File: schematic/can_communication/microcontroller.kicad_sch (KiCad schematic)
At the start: 1 part, among them U1 STM32H723ZGTx

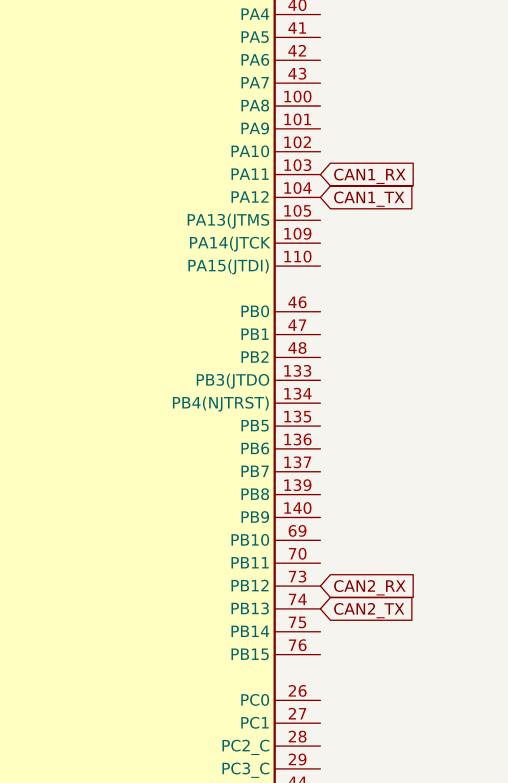
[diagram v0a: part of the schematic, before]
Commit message: added usb connectors
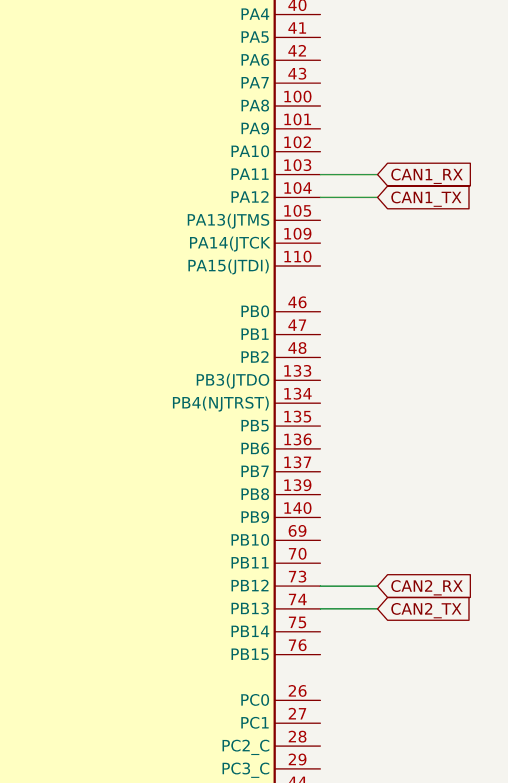
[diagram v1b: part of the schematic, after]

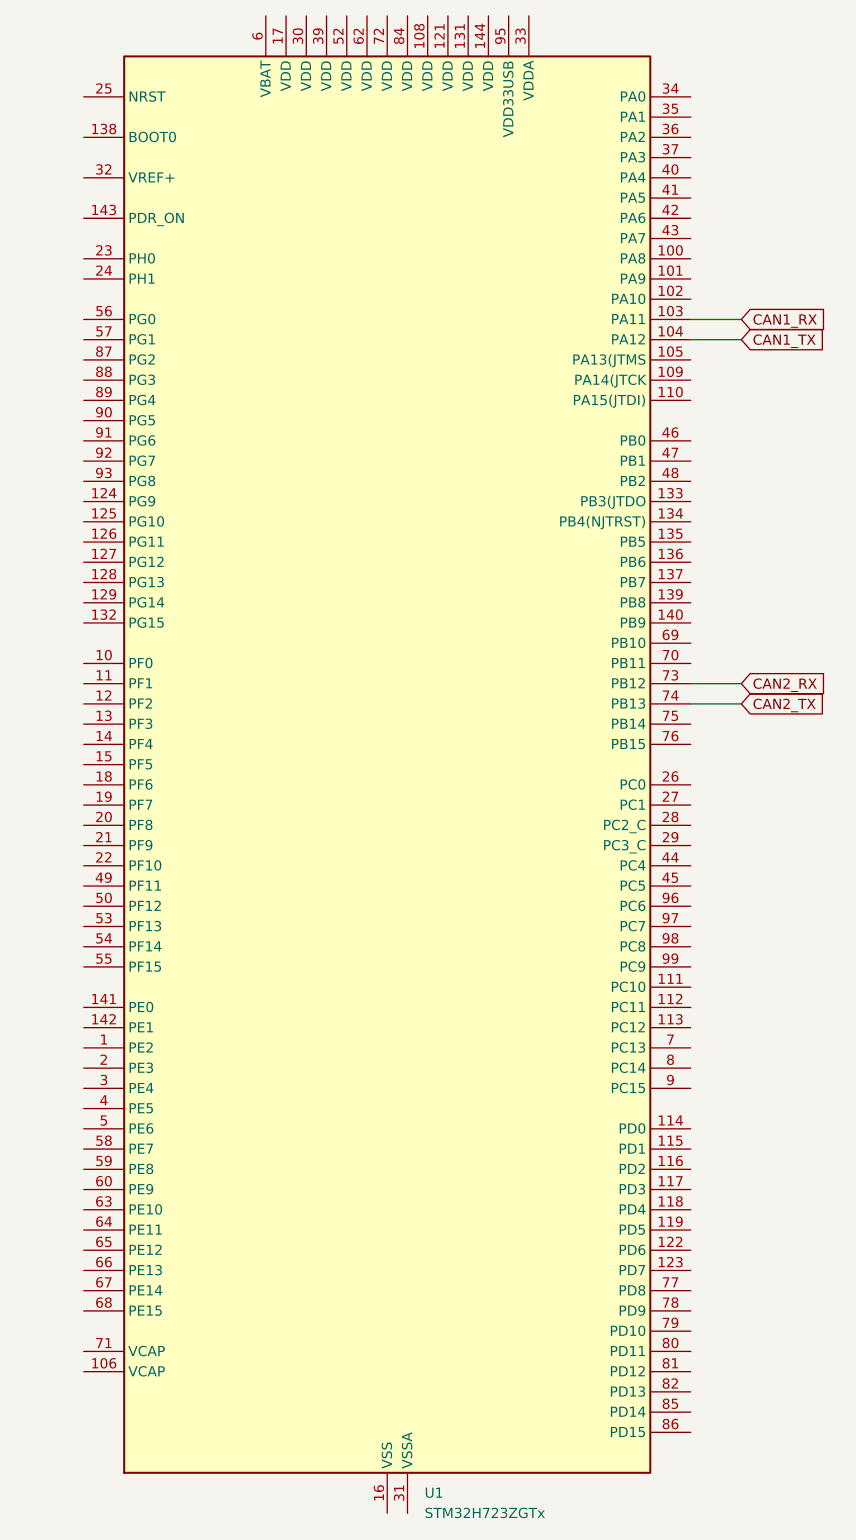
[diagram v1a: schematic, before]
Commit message: added usb connectors
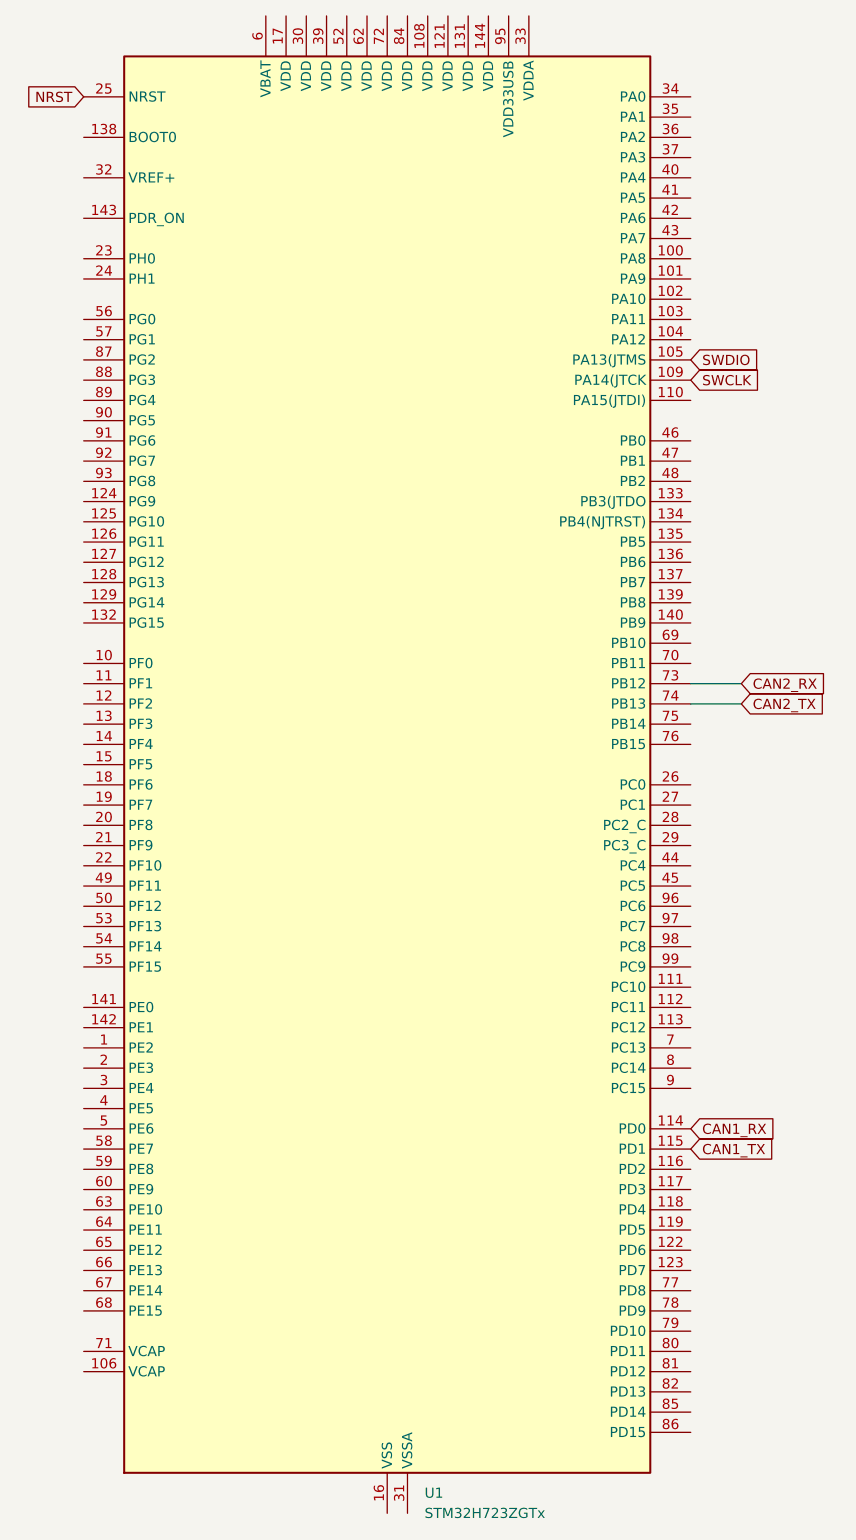
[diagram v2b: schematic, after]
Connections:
- net CAN1_RX: now also U1.114 (PD0); no longer U1.103 (PA11)
- net CAN1_TX: now also U1.115 (PD1); no longer U1.104 (PA12)
- net SWDIO: now reaches U1.105 (PA13(JTMS)
- net SWCLK: now reaches U1.109 (PA14(JTCK)
- net NRST: now reaches U1.25 (NRST)

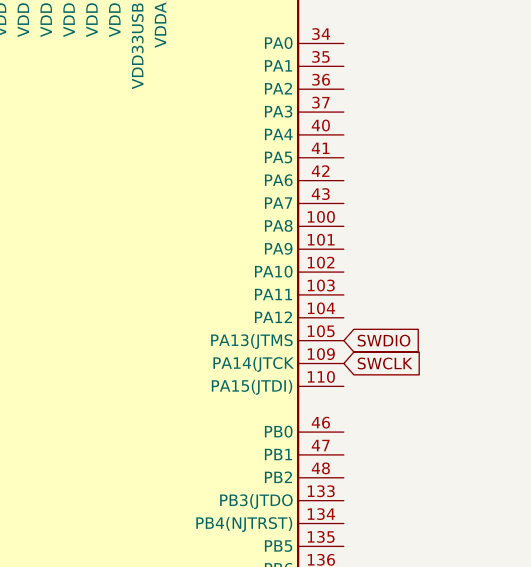
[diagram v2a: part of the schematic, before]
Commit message: added neccessary connection for stm32h7
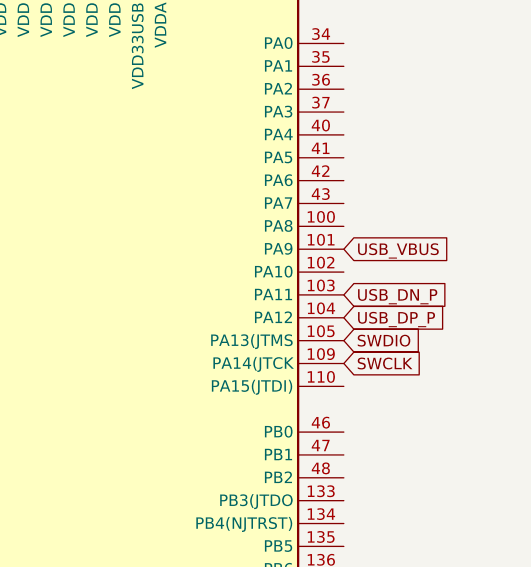
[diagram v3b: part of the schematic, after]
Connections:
- net USB_VBUS: now reaches U1.101 (PA9)
- net USB_DN_P: now reaches U1.103 (PA11)
- net USB_DP_P: now reaches U1.104 (PA12)
